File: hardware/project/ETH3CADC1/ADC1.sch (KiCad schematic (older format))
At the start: 45 parts, among them U201 DG211B, U202 OPA2192, U203 DG419xY, U204 LT5400-100k-100k, U205 LT5400-5k-1k, U206 OPA177, U207 OPA140, U208 OPA192, U209 LT5400-10k-10k, U210 LM311

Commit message: PCB layout
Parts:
- added R201: 10M, Resistor_SMD:R_0603_1608Metric_Pad0.98x0.95mm_HandSolder, symbol Device:R
- added R214, R215, R216: 10k, Resistor_SMD:R_0402_1005Metric_Pad0.72x0.64mm_HandSolder, symbol Device:R
- added U201: DG211, Package_SO:TSSOP-16_4.4x5mm_P0.65mm, symbol ETH3CDAQ1:DG211
- added U205: OPA140, Package_SO:SOIC-8_3.9x4.9mm_P1.27mm, symbol ETH3CDAQ1:OPA140
- renumbered C208 to C207, C209 to C208, C210 to C209, C207 to C210, C214 to C213, C216 to C214, C217 to C215, C213 to C216, C215 to C217, C221 to C220, C220 to C221, R201 to R202, R202 to R203, R203 to R204, R204 to R205, R205 to R206, R206 to R207, R207 to R208, R208 to R209, R209 to R210, R210 to R211, R211 to R212, R212 to R213, U201 to U202, U202 to U203, U203 to U204, U204 to U206, U205 to U207, U206 to U208, U207 to U209, U208 to U210, U209 to U211, U210 to U212
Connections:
- net +18VF: now also U201.13 (V+), U205.7 (V+)
- net +5VF: now also U201.12 (VL)
- net -14VF: now also U201.4 (V-), U205.4 (V-)
- net ADIN1: now also U201.2; no longer U206.8
- net AGNDF: now also R201.2, R214.2, U201.5 (GND)
- new net: U205.2 (-), U205.6, U206.8
- new net: R201.1, U201.10, U201.3, U201.6, U205.3 (+)
- new net: R216.1, U201.16
- new net: R215.1, U201.11
- new net: R214.1, U201.7
- new net +5V: R216.2
- no-connect marks 3 -> 7
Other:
- moved on the sheet: C201, C202, C203, C204, C205, C206, C207, C208, C209, C210, C211, C212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

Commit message: PCB modifications
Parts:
- removed C217: DNP, Capacitor_SMD:C_0402_1005Metric_Pad0.74x0.62mm_HandSolder, symbol Device:C
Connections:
- no-connect marks 7 -> 9
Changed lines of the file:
@@
 	-1   0    0    1
-$EndComp
-Wire Wire Line
-	9750 2450 9750 2550
-Wire Wire Line
-	10300 2450 9750 2450
-Wire Wire Line
-	10300 3300 10300 2450
-Wire Wire Line
-	10200 3300 10300 3300
-Wire Wire Line
-	9750 3300 9900 3300
-Wire Wire Line
-	9750 3150 9750 3300
-$Comp
-L Device:C C217
-U 1 1 605730A7
-P 10050 3300
-F 0 "C217" V 9798 3300 50  0000 C CNN
-F 1 "DNP" V 9889 3300 50  0000 C CNN
-F 2 "Capacitor_SMD:C_0402_1005Metric_Pad0.74x0.62mm_HandSolder" H 10088 3150 50  0001 C CNN
-F 3 "~" H 10050 3300 50  0001 C CNN
-	1    10050 3300
-	0    1    1    0
 $EndComp
 $Comp
@@
 	-1   0    0    1
 $EndComp
+NoConn ~ 9750 3150
+NoConn ~ 9750 2550
 $EndSCHEMATC

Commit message: PCB modifications
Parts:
- renumbered C210 to C209, C209 to C210, C216 to C215, C215 to C216, C218 to C217, C219 to C218, C220 to C219, C221 to C220, R214 to R201, R215 to R202, R216 to R203, R201 to R204, R202 to R205, R203 to R206, R204 to R207, R205 to R208, R206 to R209, R207 to R210, R208 to R211, R209 to R212, R210 to R213, R211 to R214, R212 to R215, R213 to R216

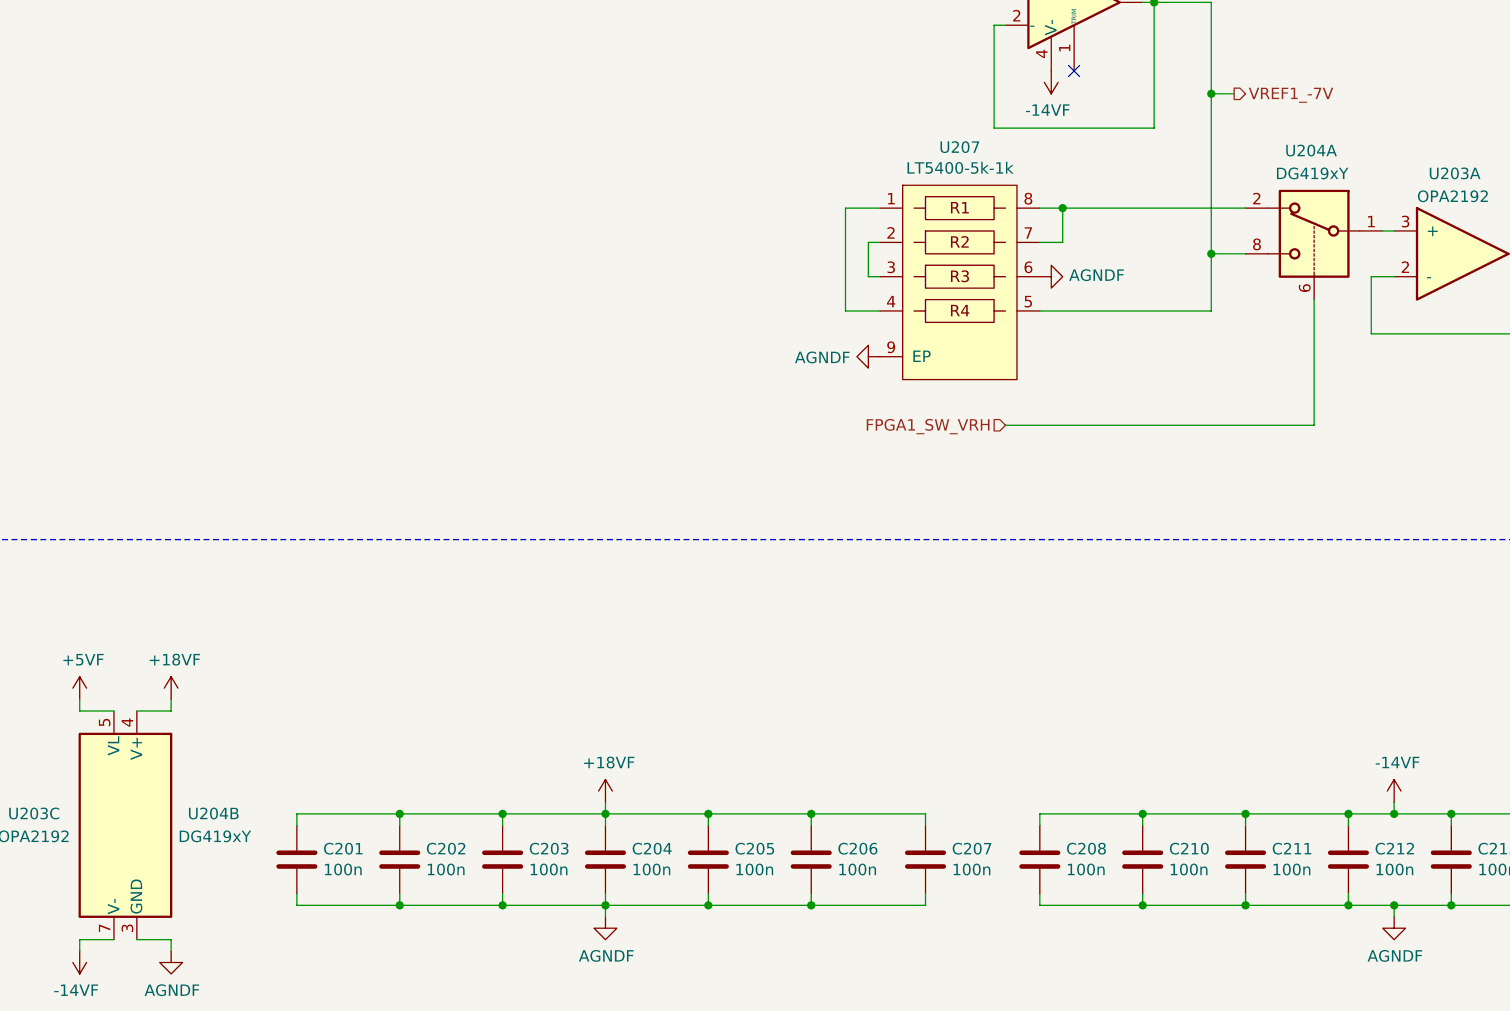
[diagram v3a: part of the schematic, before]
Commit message: Fixed mistake with DG419. Never use DG419Lxx variant.
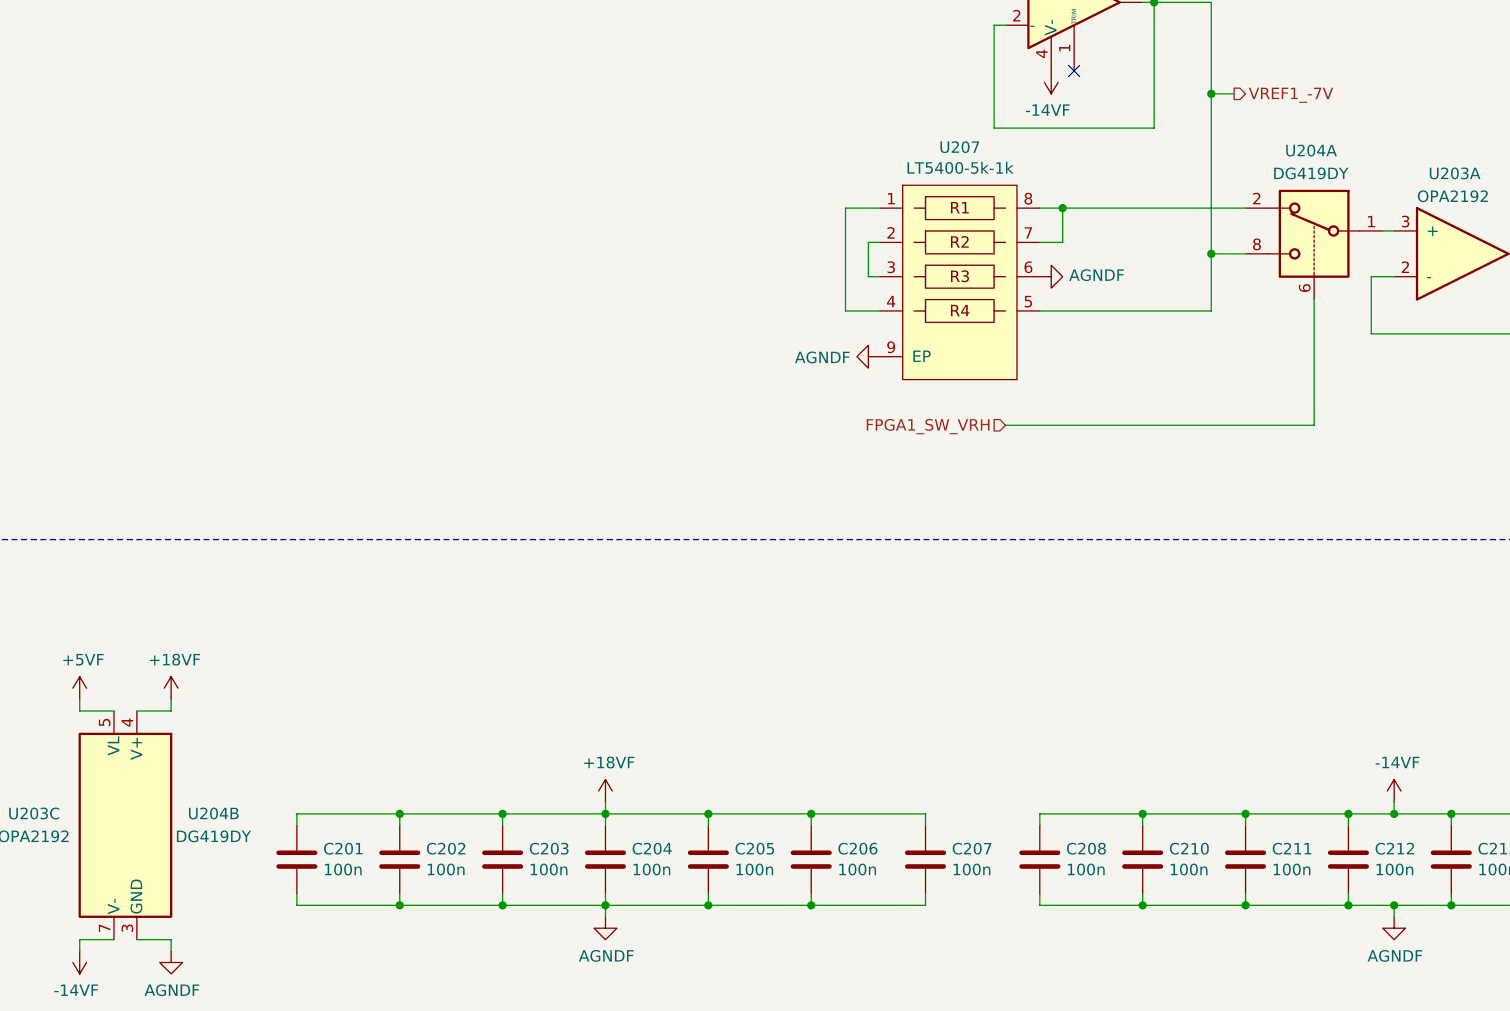
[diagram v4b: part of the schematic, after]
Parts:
- U204: value DG419xY -> DG419DY
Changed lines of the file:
@@
 P 3400 10350
 F 0 "U204" H 2950 10400 50  0000 L CNN
-F 1 "DG419xY" H 2900 10300 50  0000 L CNN
+F 1 "DG419DY" H 2900 10300 50  0000 L CNN
 F 2 "Package_SO:SOIC-8_3.9x4.9mm_P1.27mm" H 3400 10050 50  0001 C CNN
 F 3 "https://datasheets.maximintegrated.com/en/ds/DG417-DG419.pdf" H 3400 10350 50  0001 C CNN
@@
 P 8550 7650
 F 0 "U204" H 8450 7900 50  0000 L CNN
-F 1 "DG419xY" H 8400 7800 50  0000 L CNN
+F 1 "DG419DY" H 8400 7800 50  0000 L CNN
 F 2 "Package_SO:SOIC-8_3.9x4.9mm_P1.27mm" H 8550 7350 50  0001 C CNN
 F 3 "https://datasheets.maximintegrated.com/en/ds/DG417-DG419.pdf" H 8550 7650 50  0001 C CNN

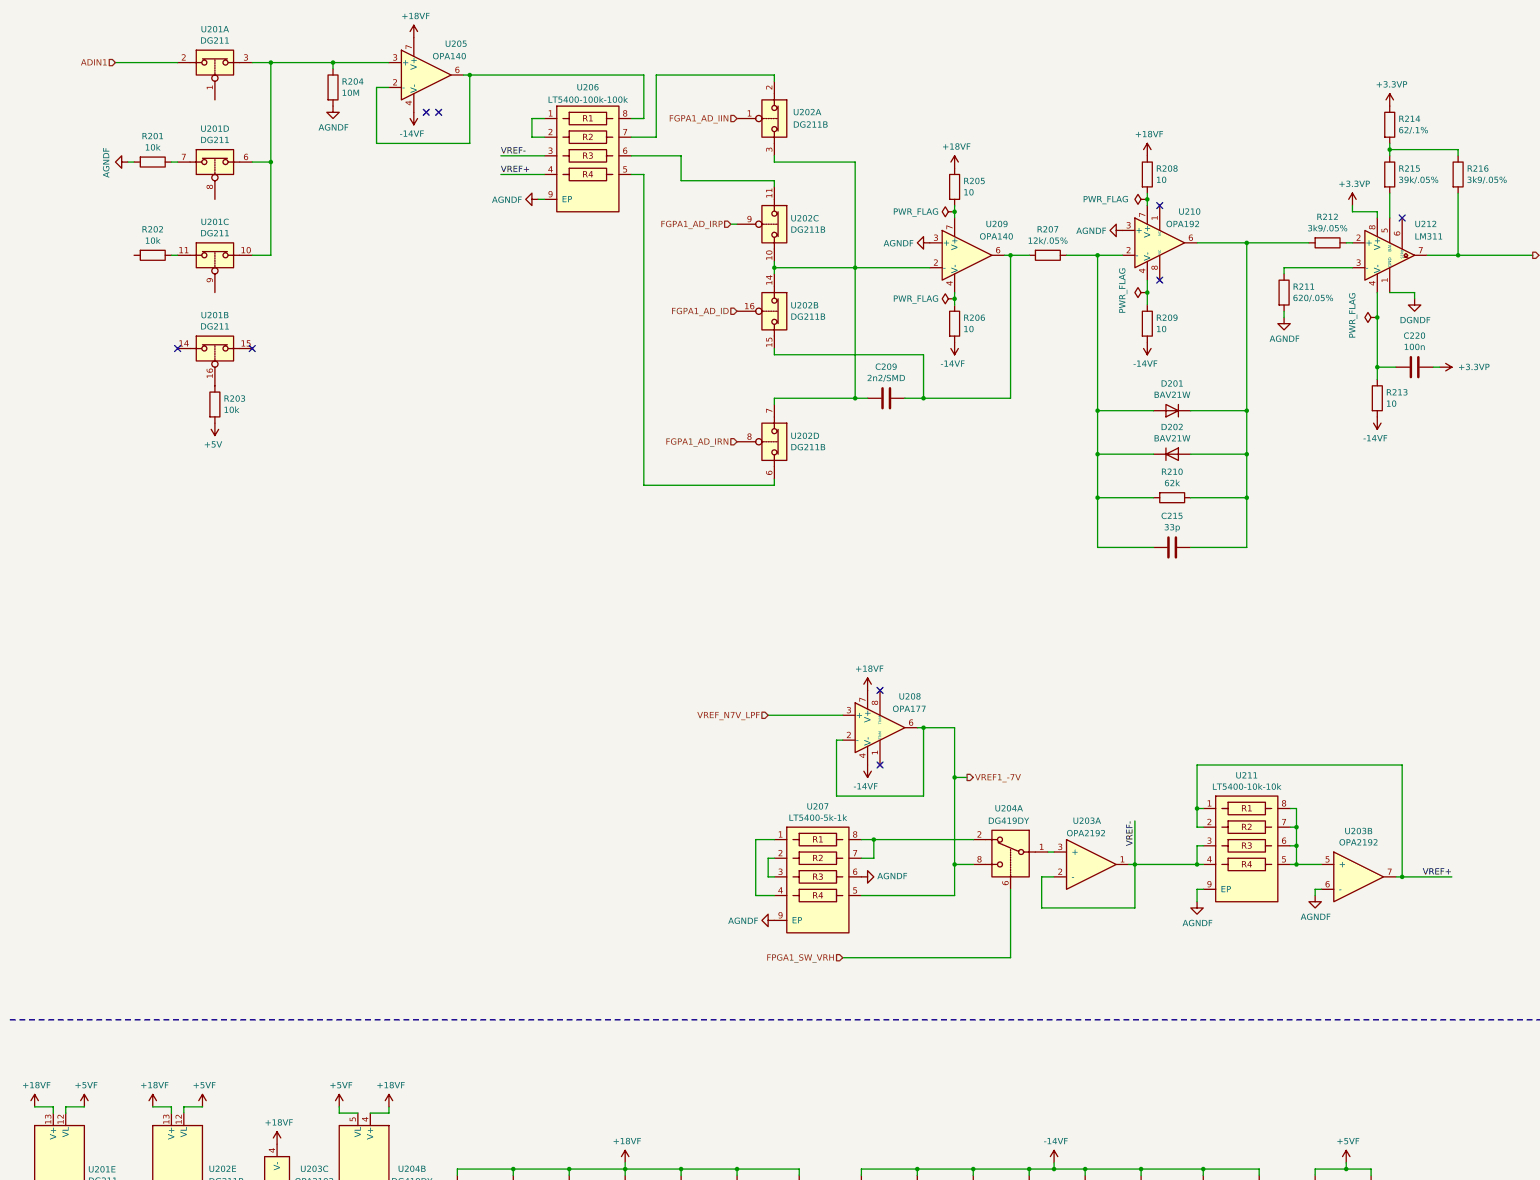
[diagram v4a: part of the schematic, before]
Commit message: SDRAM works, thanks to the website https://medium.com/@pjinwoo123/stm32h7-external-sdram-evaluation-board-cc72444898d8 . Modified the code to work with SDRAM BANK2. SCPI library works.
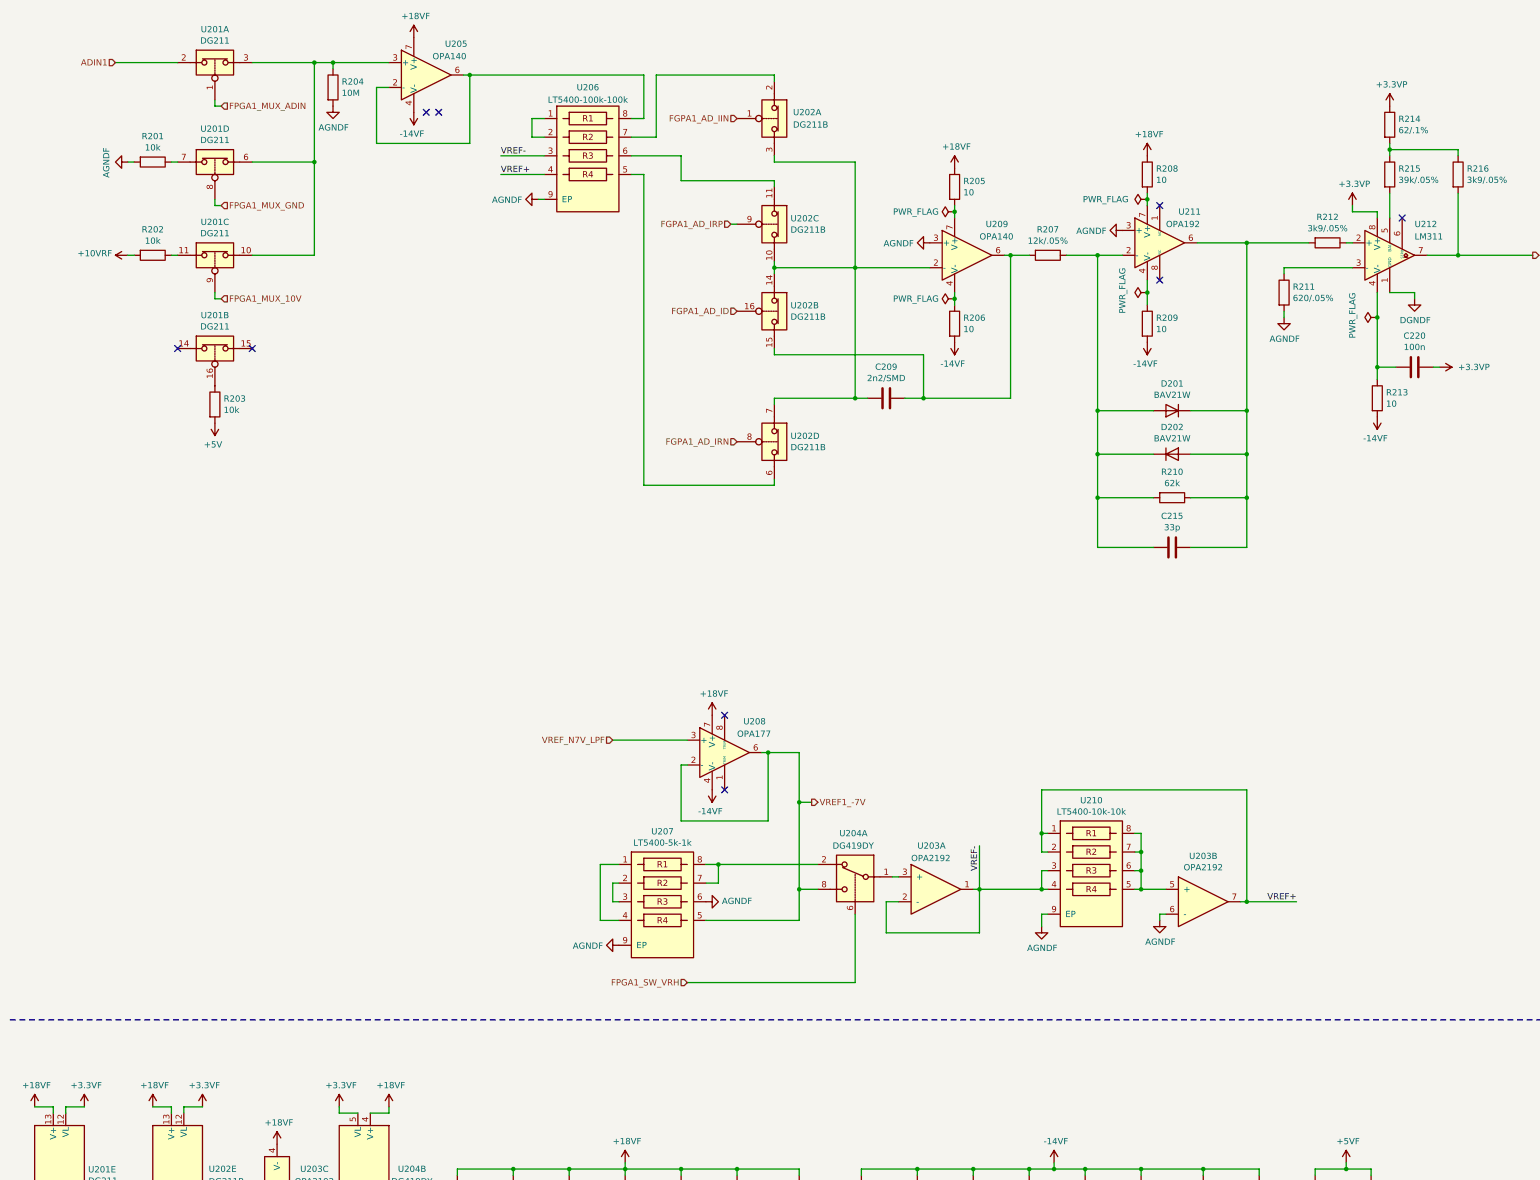
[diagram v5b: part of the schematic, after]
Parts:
- renumbered U211 to U210, U210 to U211
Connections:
- net +5VF: no longer U201.12 (VL), U202.12 (VL), U204.5 (VL)
- net FPGA1_MUX_ADIN: now reaches U201.1
- net FPGA1_MUX_10V: now reaches U201.9
- net FPGA1_MUX_GND: now reaches U201.8
- net +10VRF: now reaches R202.2
- new net +3.3VF: U201.12 (VL), U202.12 (VL), U204.5 (VL)
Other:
- moved on the sheet: U203A, U203B, U204A, U207, U208, U210
